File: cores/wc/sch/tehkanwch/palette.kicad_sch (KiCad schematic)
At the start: 21 parts

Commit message: wc: scroll visible (scene 3)
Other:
- note removed: "DAUGHTER24"
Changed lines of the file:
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@@
-		)
-	)
-	(text "DAUGHTER24"
-		(exclude_from_sim no)
-		(at 101.854 94.488 0)
-		(effects
-			(font
-				(size 1.27 1.27)
-			)
 		)
 	)

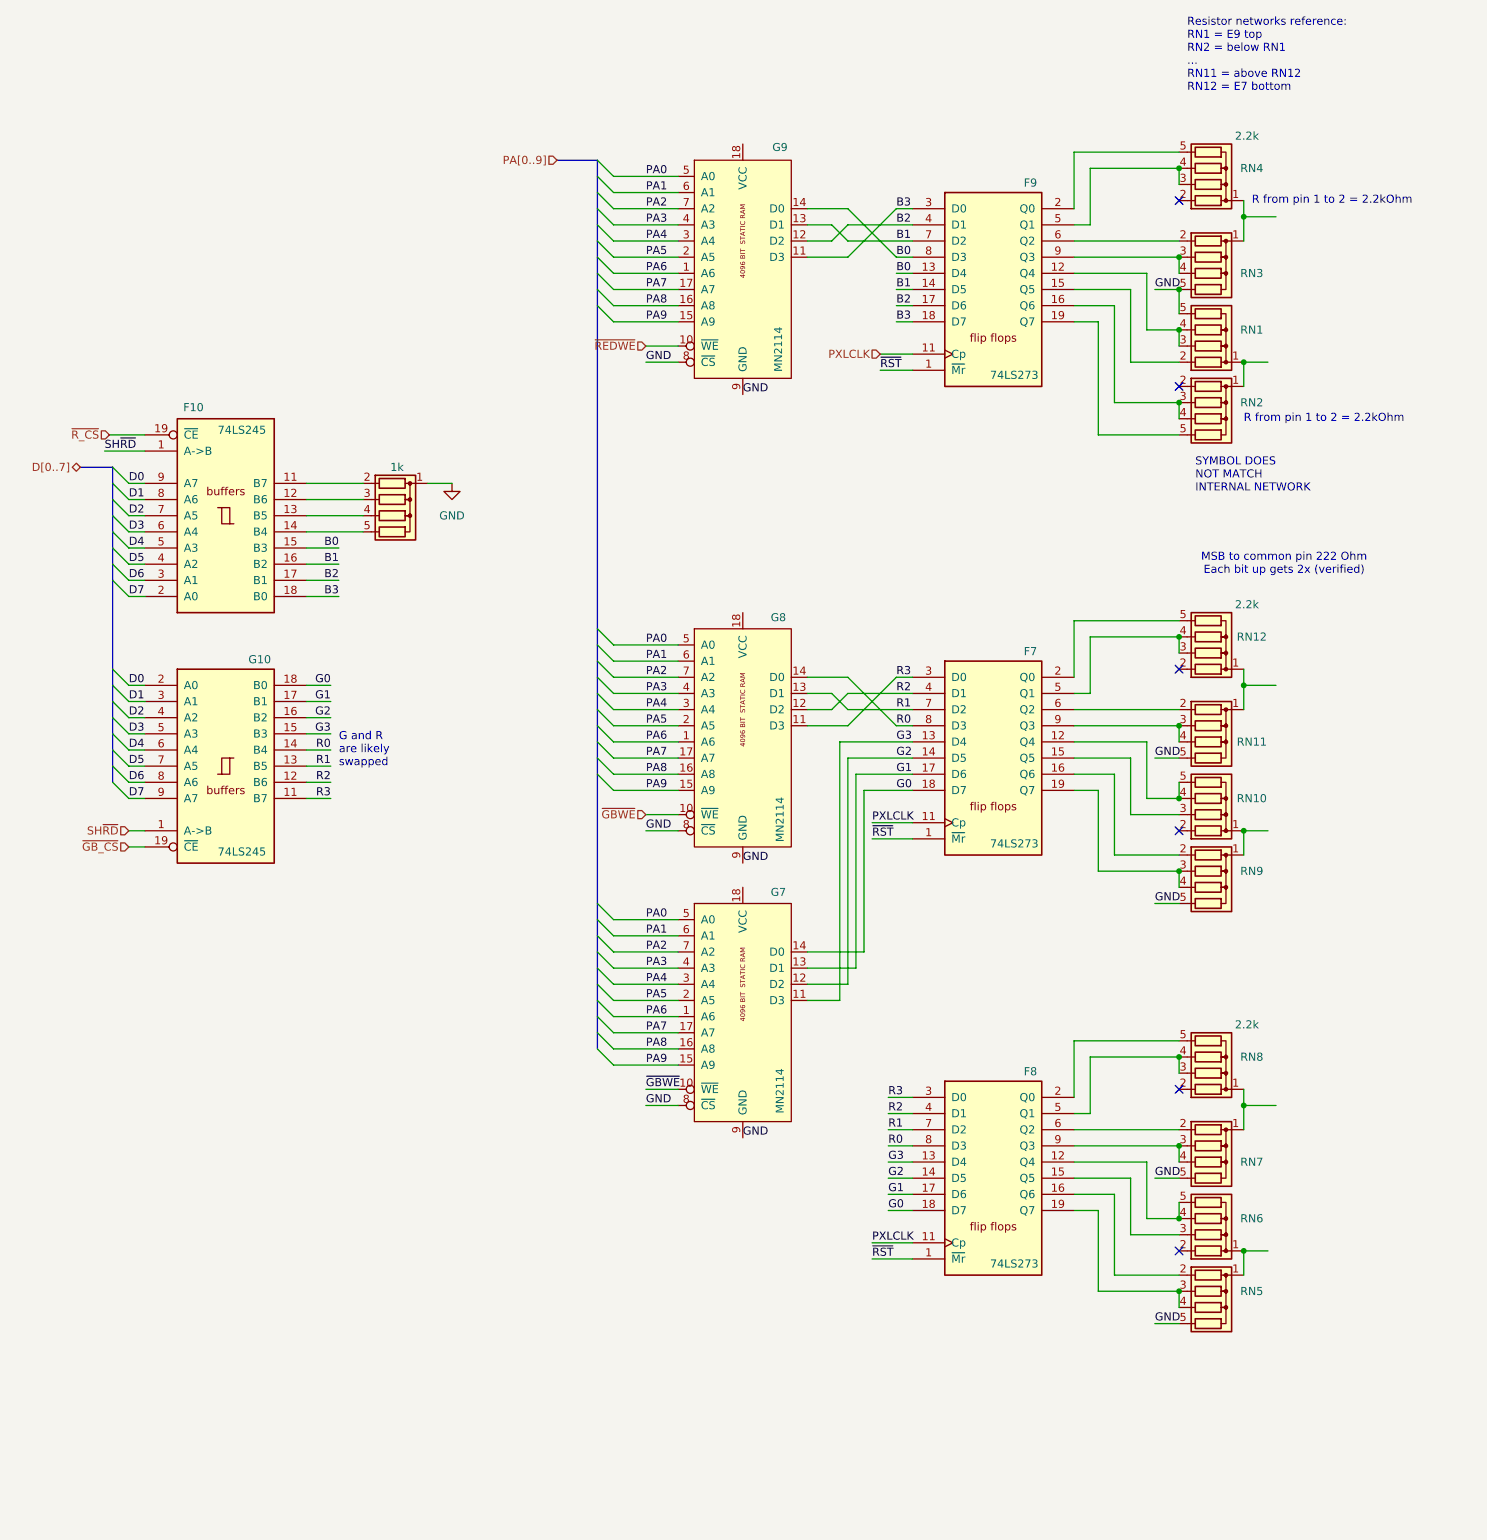
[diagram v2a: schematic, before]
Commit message: tehkanwch: edge connector pin names
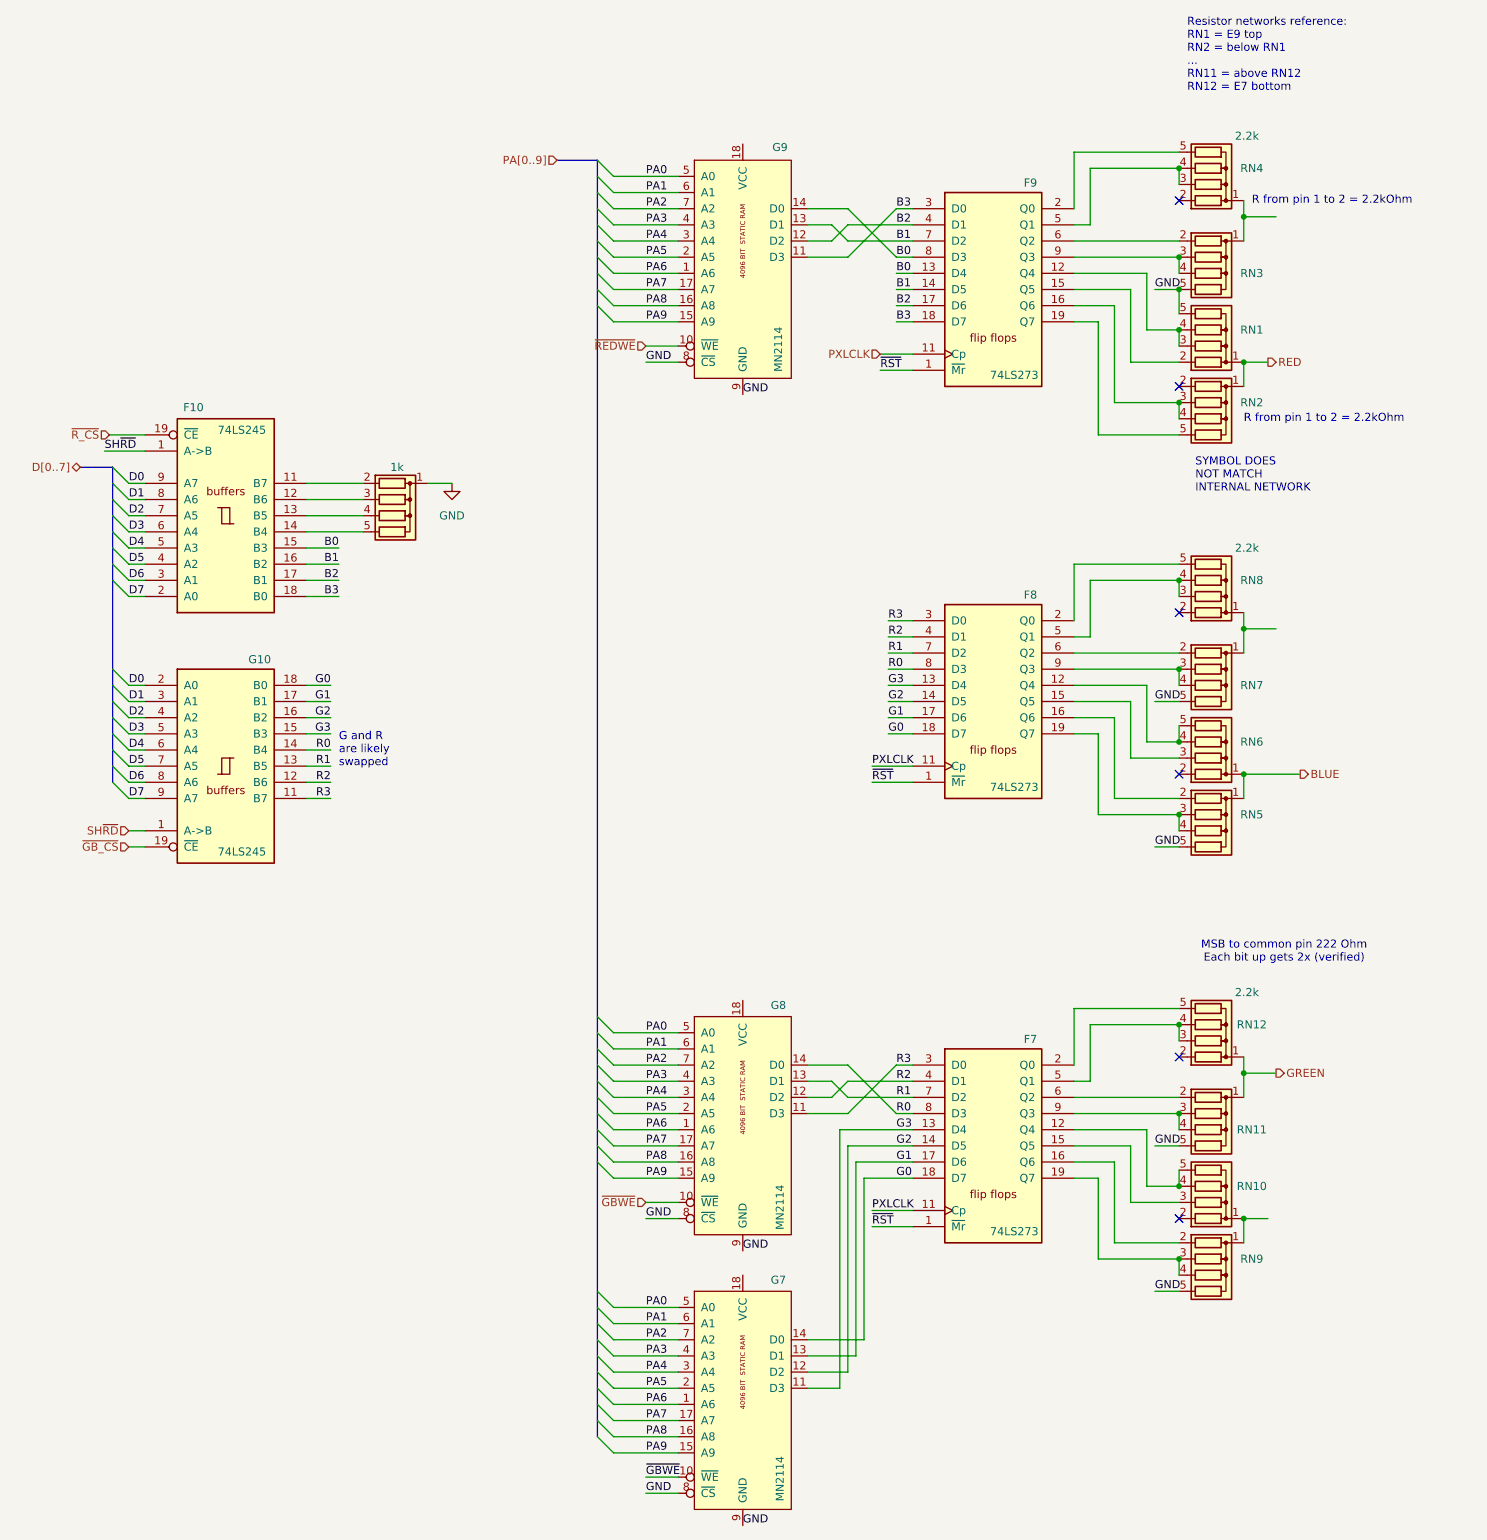
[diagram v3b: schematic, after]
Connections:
- net BLUE: now reaches RN5.1 (common), RN6.1 (common)
- net RED: now reaches RN1.1 (common), RN2.1 (common)
- net GREEN: now reaches RN11.1 (common), RN12.1 (common)
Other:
- moved on the sheet: F7, F8, G7, G8, RN10, RN11, RN12, RN5, RN6, RN7, RN8, RN9

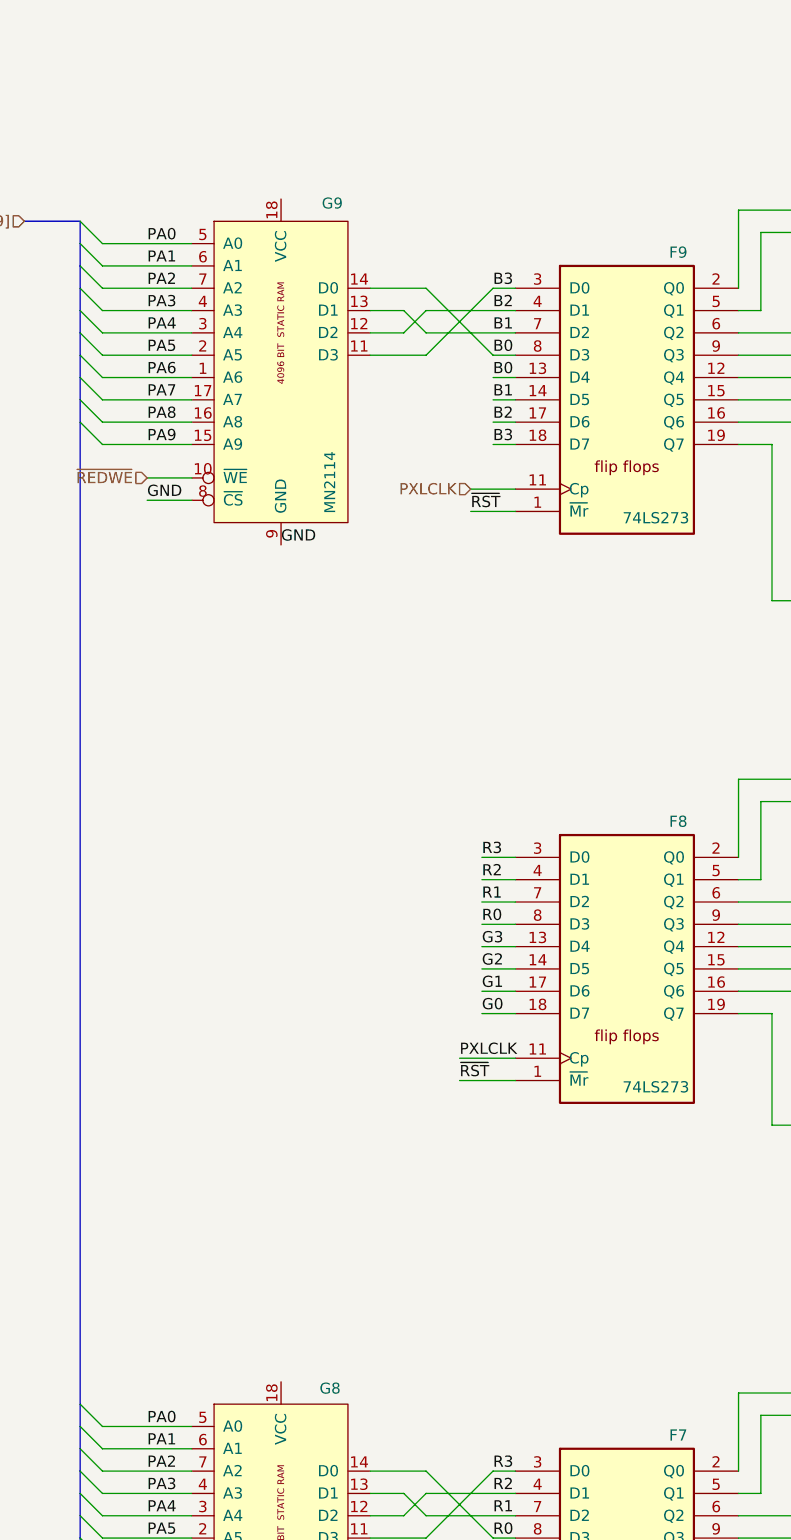
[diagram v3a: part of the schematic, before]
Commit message: wc: support for analog gamepad
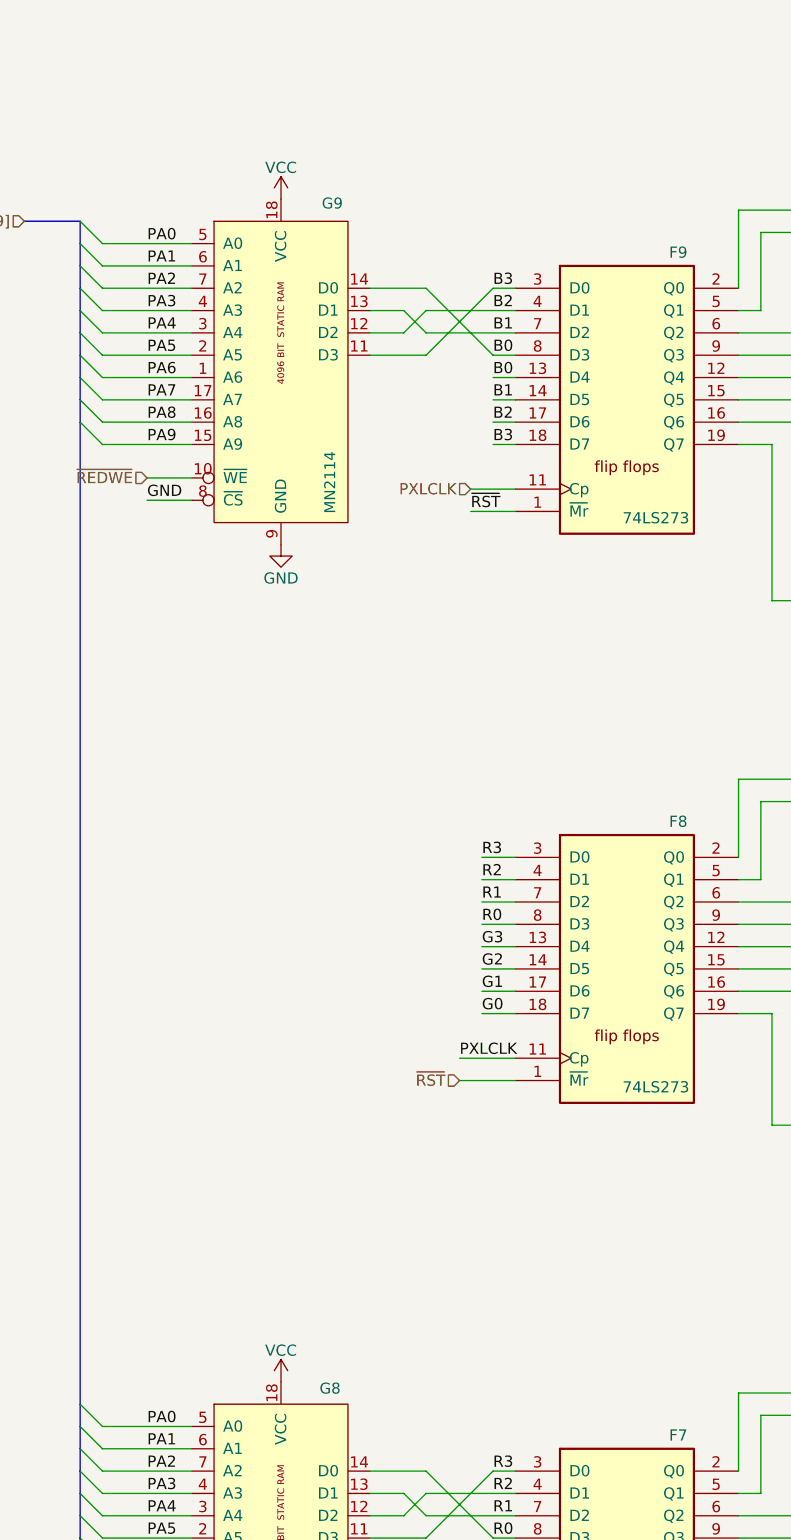
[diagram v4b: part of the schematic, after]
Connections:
- net VCC: now reaches G8.18 (VCC)
- net VCC: now also G9.18 (VCC)
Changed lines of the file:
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@@
-		)
-	)
-	(label "GND"
-		(at 204.47 95.25 0)
-		(fields_autoplaced yes)
-		(effects
-			(font
-				(size 1.27 1.27)
-			)
-			(justify left bottom)
 		)
 	)
@@
 			)
 			(justify right bottom)
-		)
-	)
-	(label "~{RST}"
-		(at 224.79 156.21 0)
-		(fields_autoplaced yes)
-		(effects
-			(font
-				(size 1.27 1.27)
-			)
-			(justify left bottom)
 		)
 	)
@@
 		(shape bidirectional)
 		(at 100.33 106.68 180)
+		(fields_autoplaced yes)
+		(effects
+			(font
+				(size 1.27 1.27)
+			)
+			(justify right)
+		)
+	)
+	(hierarchical_label "~{RST}"
+		(shape input)
+		(at 224.79 156.21 180)
 		(fields_autoplaced yes)
 		(effects
@@
 				(path "/f324726e-ed6b-4b88-9562-4b07e126a276/4d18f4f6-4d7d-4823-941f-121a8e5c871f/e275c20e-58da-4787-bf27-1e3b67330979"
 					(reference "F9")
+					(unit 1)
+				)
+			)
+		)
+	)
+	(symbol
+		(lib_id "power:VCC")
+		(at 204.47 55.88 0)
+		(unit 1)
+		(exclude_from_sim no)
+		(in_bom yes)
+		(on_board yes)
+		(dnp no)
+		(property "Reference" "#PWR083"
+			(at 204.47 59.69 0)
+			(effects
+				(font
+					(size 1.27 1.27)
+				)
+				(hide yes)
+			)
+		)
+		(property "Value" "VCC"
+			(at 204.47 52.324 0)
+			(effects
+				(font
+					(size 1.27 1.27)
+				)
+			)
+		)
+		(property "Footprint" ""
+			(at 204.47 55.88 0)
+			(effects
+				(font
+					(size 1.27 1.27)
+				)
+				(hide yes)
+			)
+		)
+		(property "Datasheet" ""
+			(at 204.47 55.88 0)
+			(effects
+				(font
+					(size 1.27 1.27)
+				)
+				(hide yes)
+			)
+		)
+		(property "Description" "Power symbol creates a global label with name \"VCC\""
+			(at 204.47 55.88 0)
+			(effects
+				(font
+					(size 1.27 1.27)
+				)
+				(hide yes)
+			)
+		)
+		(pin "1"
+		)
+		(instances
+			(project ""
+				(path "/f324726e-ed6b-4b88-9562-4b07e126a276/4d18f4f6-4d7d-4823-941f-121a8e5c871f/e275c20e-58da-4787-bf27-1e3b67330979"
+					(reference "#PWR083")
 					(unit 1)
 				)
@@
 	)
 	(symbol
+		(lib_id "power:VCC")
+		(at 204.47 190.5 0)
+		(unit 1)
+		(exclude_from_sim no)
+		(in_bom yes)
+		(on_board yes)
+		(dnp no)
+		(property "Reference" "#PWR082"
+			(at 204.47 194.31 0)
+			(effects
+				(font
+					(size 1.27 1.27)
+				)
+				(hide yes)
+			)
+		)
+		(property "Value" "VCC"
+			(at 204.47 186.944 0)
+			(effects
+				(font
+					(size 1.27 1.27)
+				)
+			)
+		)
+		(property "Footprint" ""
+			(at 204.47 190.5 0)
+			(effects
+				(font
+					(size 1.27 1.27)
+				)
+				(hide yes)
+			)
+		)
+		(property "Datasheet" ""
+			(at 204.47 190.5 0)
+			(effects
+				(font
+					(size 1.27 1.27)
+				)
+				(hide yes)
+			)
+		)
+		(property "Description" "Power symbol creates a global label with name \"VCC\""
+			(at 204.47 190.5 0)
+			(effects
+				(font
+					(size 1.27 1.27)
+				)
+				(hide yes)
+			)
+		)
+		(pin "1"
+		)
+		(instances
+			(project ""
+				(path "/f324726e-ed6b-4b88-9562-4b07e126a276/4d18f4f6-4d7d-4823-941f-121a8e5c871f/e275c20e-58da-4787-bf27-1e3b67330979"
+					(reference "#PWR082")
+					(unit 1)
+				)
+			)
+		)
+	)
+	(symbol
 		(lib_id "jt74:74LS245")
 		(at 123.19 153.67 0)
@@
 					(unit 1)
 				)
+			)
+		)
+	)
+	(symbol
+		(lib_id "power:GND")
+		(at 204.47 95.25 0)
+		(unit 1)
+		(exclude_from_sim no)
+		(in_bom yes)
+		(on_board yes)
+		(dnp no)
+		(property "Reference" "#PWR084"
+			(at 204.47 101.6 0)
+			(effects
+				(font
+					(size 1.27 1.27)
+				)
+				(hide yes)
+			)
+		)
+		(property "Value" "GND"
+			(at 204.47 99.06 0)
+			(effects
+				(font
+					(size 1.27 1.27)
+				)
+			)
+		)
+		(property "Footprint" ""
+			(at 204.47 95.25 0)
+			(effects
+				(font
+					(size 1.27 1.27)
+				)
+				(hide yes)
+			)
+		)
+		(property "Datasheet" ""
+			(at 204.47 95.25 0)
+			(effects
+				(font
+					(size 1.27 1.27)
+				)
+				(hide yes)
+			)
+		)
+		(property "Description" "Power symbol creates a global label with name \"GND\" , ground"
+			(at 204.47 95.25 0)
+			(effects
+				(font
+					(size 1.27 1.27)
+				)
+				(hide yes)
+			)
+		)
+		(pin "1"
+		)
+		(instances
+			(project ""
+				(path "/f324726e-ed6b-4b88-9562-4b07e126a276/4d18f4f6-4d7d-4823-941f-121a8e5c871f/e275c20e-58da-4787-bf27-1e3b67330979"
+					(reference "#PWR084")
+					(unit 1)
+				)
